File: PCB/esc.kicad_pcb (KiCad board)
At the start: 4 copper layers, 43.5 x 65 mm, 70 parts, among them J1 Conn_01x04_Pin, J2 Conn_01x01, J3 Conn_01x01, J4 Conn_01x01, J5 Conn_01x01, J6 Conn_01x01, Q1 XRS230N03C, Q2 XRS230N03C, Q3 XRS230N03C, Q4 XRS230N03C, Q5 XRS230N03C, Q6 XRS230N03C, SW1 SW_SPST, U1 STM32C031K6T6, U2 TLV76133DCY, U3 TLV9064, U4 INA180A3, U5 IRS21867S, U6 IRS21867S, U7 IRS21867S

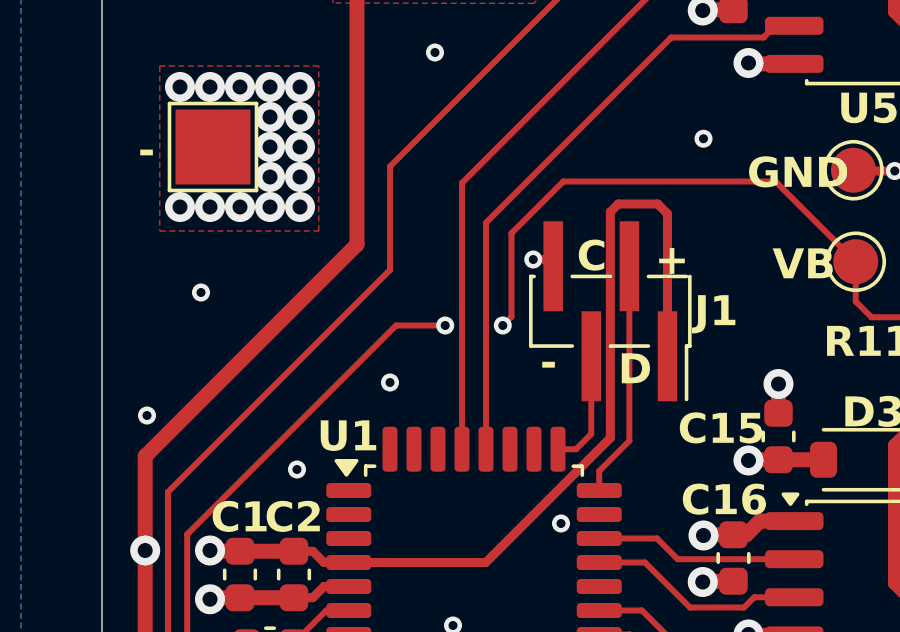
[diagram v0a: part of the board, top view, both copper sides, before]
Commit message: Switched gate driving PWM to one timer
One timer is now used so the last OC channel can be used to trigger ADC
reads on the phase voltages. In theory, haven't implemented yet.
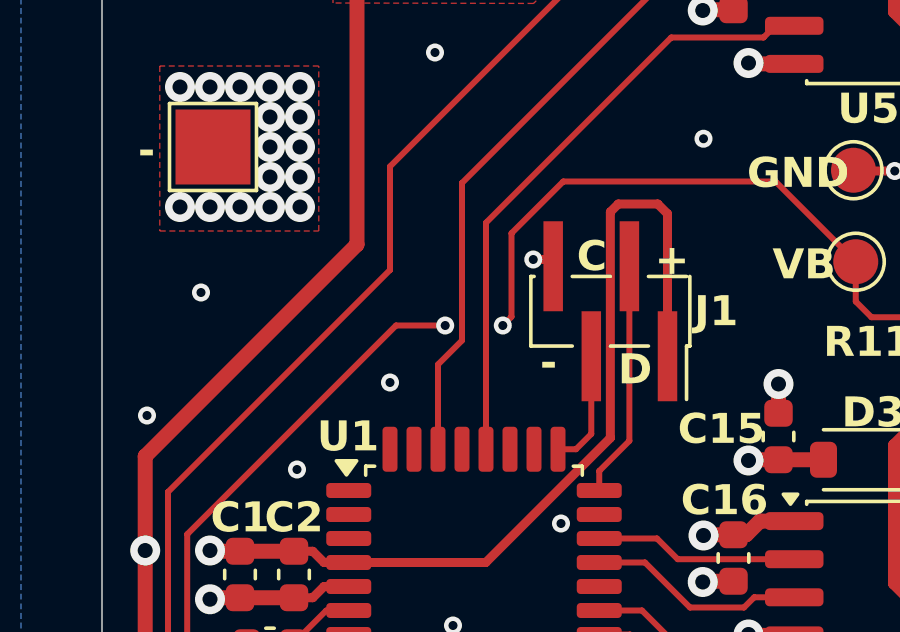
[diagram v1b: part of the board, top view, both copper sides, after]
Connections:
- U1 pad 29: /ctrl_a_h -> unconnected-(U1-PB5-Pad29)
- U1 pad 30: unconnected-(U1-PB6-Pad30) -> /ctrl_a_h
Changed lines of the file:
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@@
 			(net "unconnected-(U1-PA0-Pad7)")
 			(pinfunction "PA0_7")
-			(pintype "bidirectional")
+			(pintype "bidirectional+no_connect")
 		)
 		(pad "8" smd roundrect
@@
 			(layers "F.Cu" "F.Mask" "F.Paste")
 			(roundrect_rratio 0.25)
-			(net "/ctrl_a_h")
+			(net "unconnected-(U1-PB5-Pad29)")
 			(pinfunction "PB5_29")
-			(pintype "bidirectional")
+			(pintype "bidirectional+no_connect")
 		)
 		(pad "30" smd roundrect
@@
 			(layers "F.Cu" "F.Mask" "F.Paste")
 			(roundrect_rratio 0.25)
-			(net "unconnected-(U1-PB6-Pad30)")
+			(net "/ctrl_a_h")
 			(pinfunction "PB6_30")
-			(pintype "bidirectional+no_connect")
+			(pintype "bidirectional")
 		)
 		(pad "31" smd roundrect
@@
 	)
 	(segment
+		(start 241.51 73.74)
+		(end 235 80.25)
+		(width 0.2)
+		(layer "F.Cu")
+		(net "/ctrl_a_h")
+	)
+	(segment
 		(start 246.075 73.74)
 		(end 241.51 73.74)
@@
 	)
 	(segment
+		(start 234.2 86.3)
+		(end 234.2 89.125)
+		(width 0.2)
+		(layer "F.Cu")
+		(net "/ctrl_a_h")
+	)
+	(segment
 		(start 235 80.25)
-		(end 235 89.125)
+		(end 235 85.5)
 		(width 0.2)
 		(layer "F.Cu")
@@
 	)
 	(segment
-		(start 241.51 73.74)
-		(end 235 80.25)
+		(start 235 85.5)
+		(end 234.2 86.3)
 		(width 0.2)
 		(layer "F.Cu")
@@
 	)
 	(segment
+		(start 232.125 115.825)
+		(end 232.1 115.8)
+		(width 0.2)
+		(layer "F.Cu")
+		(net "Net-(U3A--)")
+	)
+	(segment
+		(start 232.125 117.6)
+		(end 232.125 115.825)
+		(width 0.2)
+		(layer "F.Cu")
+		(net "Net-(U3A--)")
+	)
+	(segment
+		(start 232.125 117.6)
+		(end 232.125 119.1)
+		(width 0.2)
+		(layer "F.Cu")
+		(net "Net-(U3A--)")
+	)
+	(segment
+		(start 237.25 119.2)
+		(end 237.25 118.4)
+		(width 0.2)
+		(layer "F.Cu")
+		(net "/i_sense")
+	)
+	(segment
+		(start 232.785 118.285)
+		(end 232.785 115.835)
+		(width 0.2)
+		(layer "F.Cu")
+		(net "/i_sense")
+	)
+	(segment
+		(start 233.7 119.2)
+		(end 232.785 118.285)
+		(width 0.2)
+		(layer "F.Cu")
+		(net "/i_sense")
+	)
+	(segment
+		(start 232.785 115.835)
+		(end 232.75 115.8)
+		(width 0.2)
+		(layer "F.Cu")
+		(net "/i_sense")
+	)
+	(segment
+		(start 237.65 118)
+		(end 243.9 118)
+		(width 0.2)
+		(layer "F.Cu")
+		(net "/i_sense")
+	)
+	(segment
+		(start 237.25 118.4)
+		(end 237.65 118)
+		(width 0.2)
+		(layer "F.Cu")
+		(net "/i_sense")
+	)
+	(segment
+		(start 237.25 119.2)
+		(end 233.7 119.2)
+		(width 0.2)
+		(layer "F.Cu")
+		(net "/i_sense")
+	)
+	(segment
+		(start 225.2 90.55)
+		(end 225.2 100)
+		(width 0.2)
+		(layer "F.Cu")
+		(net "/v_a")
+	)
+	(segment
+		(start 232.6 79.7)
+		(end 232.6 83.15)
+		(width 0.2)
+		(layer "F.Cu")
+		(net "/v_a")
+	)
+	(segment
+		(start 225.2 100)
+		(end 232.75 107.55)
+		(width 0.2)
+		(layer "F.Cu")
+		(net "/v_a")
+	)
+	(segment
+		(start 248.1 65.675)
+		(end 246.625 65.675)
+		(width 0.2)
+		(layer "F.Cu")
+		(net "/v_a")
+	)
+	(segment
+		(start 248.125 63.825)
+		(end 248.125 65.65)
+		(width 0.2)
+		(layer "F.Cu")
+		(net "/v_a")
+	)
+	(segment
+		(start 246.625 65.675)
+		(end 232.6 79.7)
+		(width 0.2)
+		(layer "F.Cu")
+		(net "/v_a")
+	)
+	(segment
+		(start 248.125 65.65)
+		(end 248.1 65.675)
+		(width 0.2)
+		(layer "F.Cu")
+		(net "/v_a")
+	)
+	(segment
+		(start 232.75 107.55)
+		(end 232.75 110.075)
+		(width 0.2)
+		(layer "F.Cu")
+		(net "/v_a")
+	)
+	(segment
+		(start 232.6 83.15)
+		(end 225.2 90.55)
+		(width 0.2)
+		(layer "F.Cu")
+		(net "/v_a")
+	)
+	(segment
+		(start 251.85 65.675)
+		(end 248.1 65.675)
+		(width 0.2)
+		(layer "F.Cu")
+		(net "/v_a")
+	)
+	(segment
 		(start 251.85 69.05)
 		(end 250.29145 69.05)
@@
 	)
 	(segment
-		(start 225.2 90.55)
-		(end 225.2 100)
-		(width 0.2)
-		(layer "F.Cu")
-		(net "/v_a")
-	)
-	(segment
-		(start 232.6 79.7)
-		(end 232.6 83.15)
-		(width 0.2)
-		(layer "F.Cu")
-		(net "/v_a")
-	)
-	(segment
-		(start 225.2 100)
-		(end 232.75 107.55)
-		(width 0.2)
-		(layer "F.Cu")
-		(net "/v_a")
-	)
-	(segment
-		(start 248.1 65.675)
-		(end 246.625 65.675)
-		(width 0.2)
-		(layer "F.Cu")
-		(net "/v_a")
-	)
-	(segment
-		(start 248.125 63.825)
-		(end 248.125 65.65)
-		(width 0.2)
-		(layer "F.Cu")
-		(net "/v_a")
-	)
-	(segment
-		(start 246.625 65.675)
-		(end 232.6 79.7)
-		(width 0.2)
-		(layer "F.Cu")
-		(net "/v_a")
-	)
-	(segment
-		(start 248.125 65.65)
-		(end 248.1 65.675)
-		(width 0.2)
-		(layer "F.Cu")
-		(net "/v_a")
-	)
-	(segment
-		(start 232.75 107.55)
-		(end 232.75 110.075)
-		(width 0.2)
-		(layer "F.Cu")
-		(net "/v_a")
-	)
-	(segment
-		(start 232.6 83.15)
-		(end 225.2 90.55)
-		(width 0.2)
-		(layer "F.Cu")
-		(net "/v_a")
-	)
-	(segment
-		(start 251.85 65.675)
-		(end 248.1 65.675)
-		(width 0.2)
-		(layer "F.Cu")
-		(net "/v_a")
-	)
-	(segment
 		(start 251.025 95.33)
 		(end 254.32 95.33)
@@
 	)
 	(segment
-		(start 237.25 119.2)
-		(end 237.25 118.4)
-		(width 0.2)
-		(layer "F.Cu")
-		(net "/i_sense")
-	)
-	(segment
-		(start 232.785 118.285)
-		(end 232.785 115.835)
-		(width 0.2)
-		(layer "F.Cu")
-		(net "/i_sense")
-	)
-	(segment
-		(start 233.7 119.2)
-		(end 232.785 118.285)
-		(width 0.2)
-		(layer "F.Cu")
-		(net "/i_sense")
-	)
-	(segment
-		(start 232.785 115.835)
-		(end 232.75 115.8)
-		(width 0.2)
-		(layer "F.Cu")
-		(net "/i_sense")
-	)
-	(segment
-		(start 237.65 118)
-		(end 243.9 118)
-		(width 0.2)
-		(layer "F.Cu")
-		(net "/i_sense")
-	)
-	(segment
-		(start 237.25 118.4)
-		(end 237.65 118)
-		(width 0.2)
-		(layer "F.Cu")
-		(net "/i_sense")
-	)
-	(segment
-		(start 237.25 119.2)
-		(end 233.7 119.2)
-		(width 0.2)
-		(layer "F.Cu")
-		(net "/i_sense")
-	)
-	(segment
 		(start 251.025 92.79)
 		(end 254.535 92.79)
@@
 		(net "/phase_a/ho")
 	)
-	(segment
-		(start 232.125 115.825)
-		(end 232.1 115.8)
-		(width 0.2)
-		(layer "F.Cu")
-		(net "Net-(U3A--)")
-	)
-	(segment
-		(start 232.125 117.6)
-		(end 232.125 115.825)
-		(width 0.2)
-		(layer "F.Cu")
-		(net "Net-(U3A--)")
-	)
-	(segment
-		(start 232.125 117.6)
-		(end 232.125 119.1)
-		(width 0.2)
-		(layer "F.Cu")
-		(net "Net-(U3A--)")
-	)
 	(zone
